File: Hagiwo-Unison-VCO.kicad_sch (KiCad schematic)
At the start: 50 parts, among them J1 OSC2 VOL, J2 V/OCT, J3 Eurorack, J4 OUT, J5 Display, SW1 Wave, U1 XIAO_RA4M1, U2 AMS1117-5.0, U3 TL072, U4 TL072

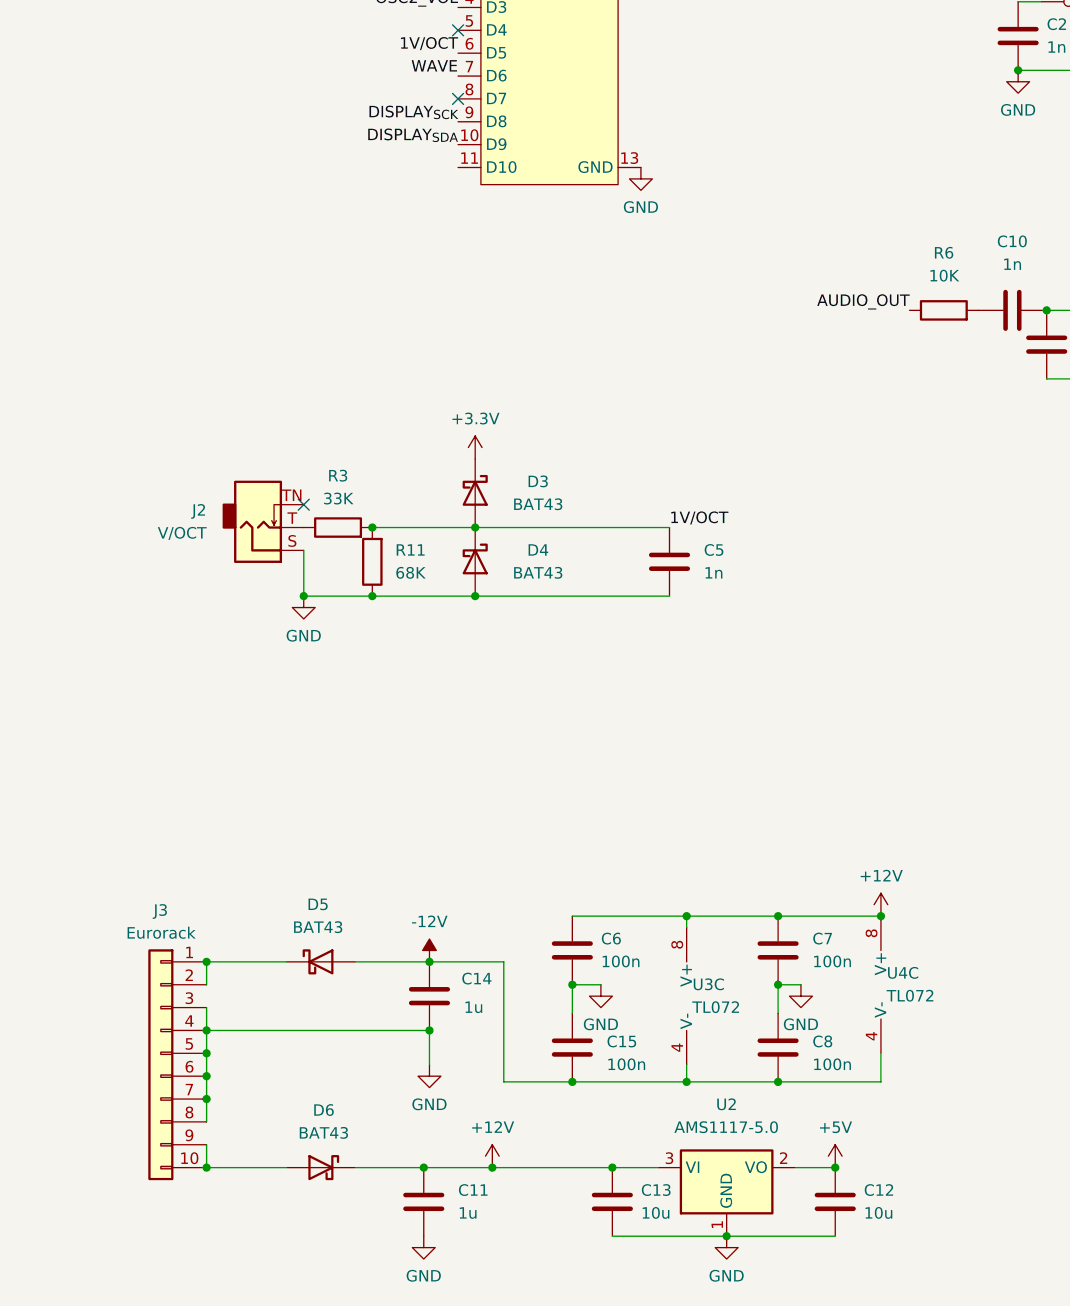
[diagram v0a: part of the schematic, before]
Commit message: add a pcb front panel
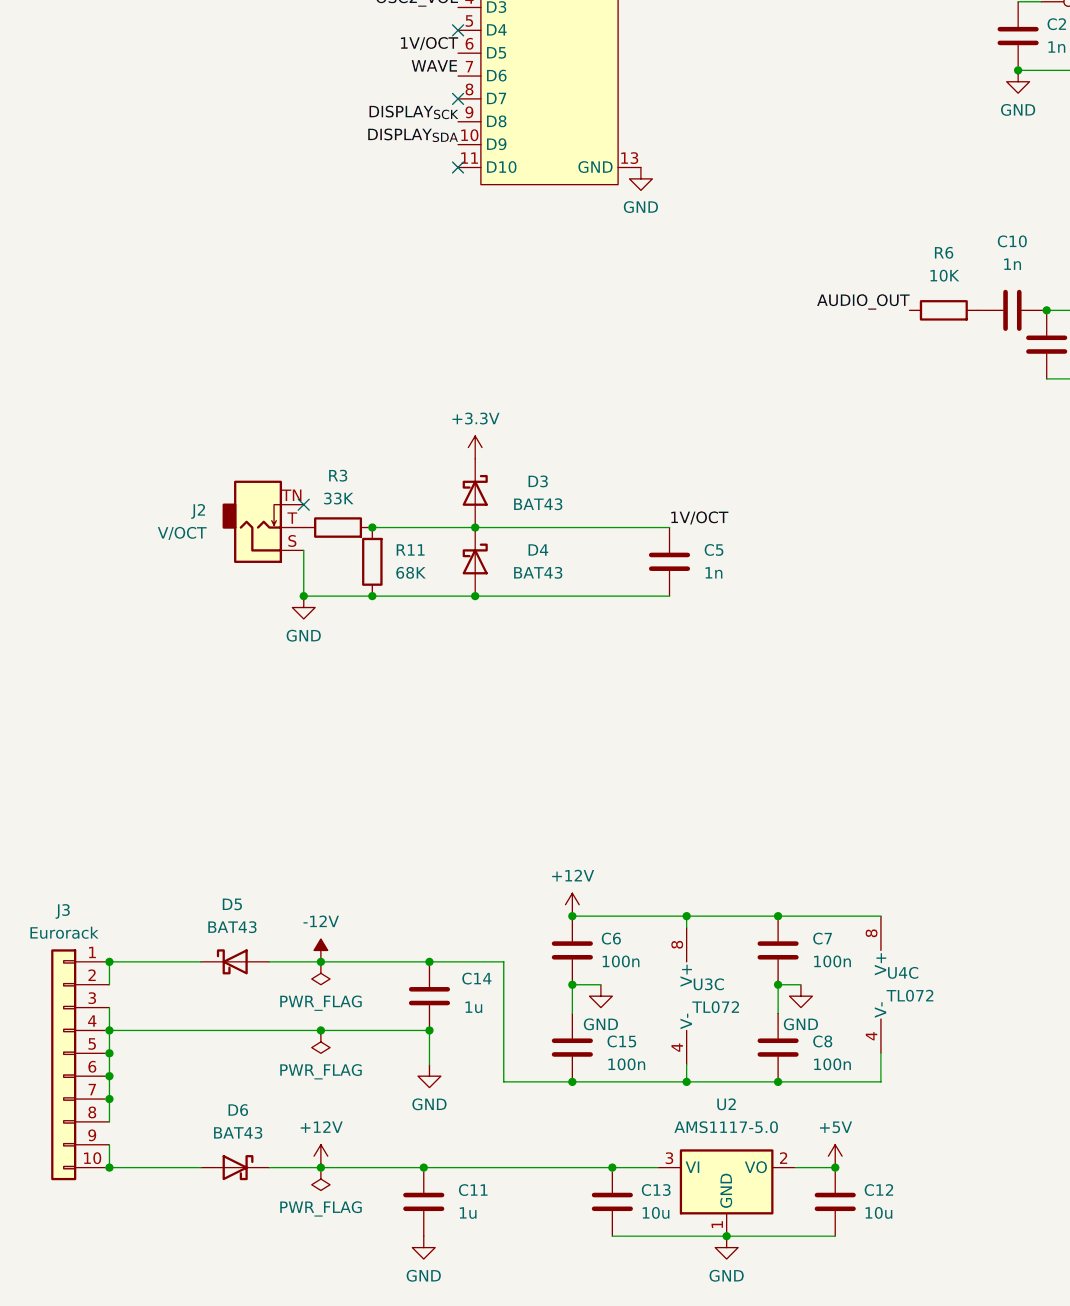
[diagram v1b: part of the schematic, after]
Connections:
- no-connect marks 5 -> 6
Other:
- moved on the sheet: D5, D6, J3
